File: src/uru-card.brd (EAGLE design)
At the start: 54 x 85.6 mm, 40 parts, among them U1 ESP32-PICO-D4, U2 MPR121QR2, U3 AP2112K-3.3TRG1, U6 ATECC508A-UDFN

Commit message: Added FT260Q USB I2C
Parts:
- added R7, R8: 22, rcl:R0603
- added R9: 5.1k, rcl:R0603
- added U4: FT260Q-T, FT260Q-T:QFN50P500X500X80-29N
- moved C6 2.37 mm to (39.6, 12.1)
- moved R2 2.37 mm to (41.6, 12.1)
- moved U2 2.12 mm to (42.0, 16.0)
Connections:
- removed net VCC: C10.1, U$1.1, U3.1, U3.3
- new net D+: R8.1, U$1.3
- new net D-: R7.1, U$1.2
- new net EXP: U4.29
- new net FSOURCE: U4.25
- new net HID_IRQ: U1.12, U4.15
- new net N$17: R9.2, U4.26
- new net N$5: R7.2, U4.20
- new net N$9: R8.2, U4.21
- new net VBUS: C10.1, R9.1, U$1.1, U3.1, U3.3
- net +3V3: now also U4.1, U4.2, U4.22, U4.23, U4.4, U4.6
- net GND: now also U4.19, U4.24, U4.5
- net RST: now also U4.3
- net SCL: now also U4.12
- net SDA: now also U4.13
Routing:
- net TOUCH_IRQ: track 36.4 -> 5.35 mm, vias 2 -> 1
- net SDA: track 105.3 -> 90.6 mm, vias 3 -> 1
- net SCL: track 104.3 -> 89.7 mm, vias 2 -> 1
- net VCC: track 13.8 -> 0.00 mm
- net VBUS: track 0.00 -> 13.8 mm
- net D+: track 0.00 -> 11.4 mm
- net D-: track 0.00 -> 10.7 mm
- net N$9: track 0.00 -> 5.33 mm
- net N$5: track 0.00 -> 4.69 mm
- net N$17: track 0.00 -> 2.90 mm
- net 8: track 35.2 -> 33.0 mm
- net 9: track 45.1 -> 42.9 mm
- net 5: track 48.3 -> 46.2 mm
- net 4: track 38.3 -> 36.2 mm
- net 3: track 72.4 -> 70.2 mm
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
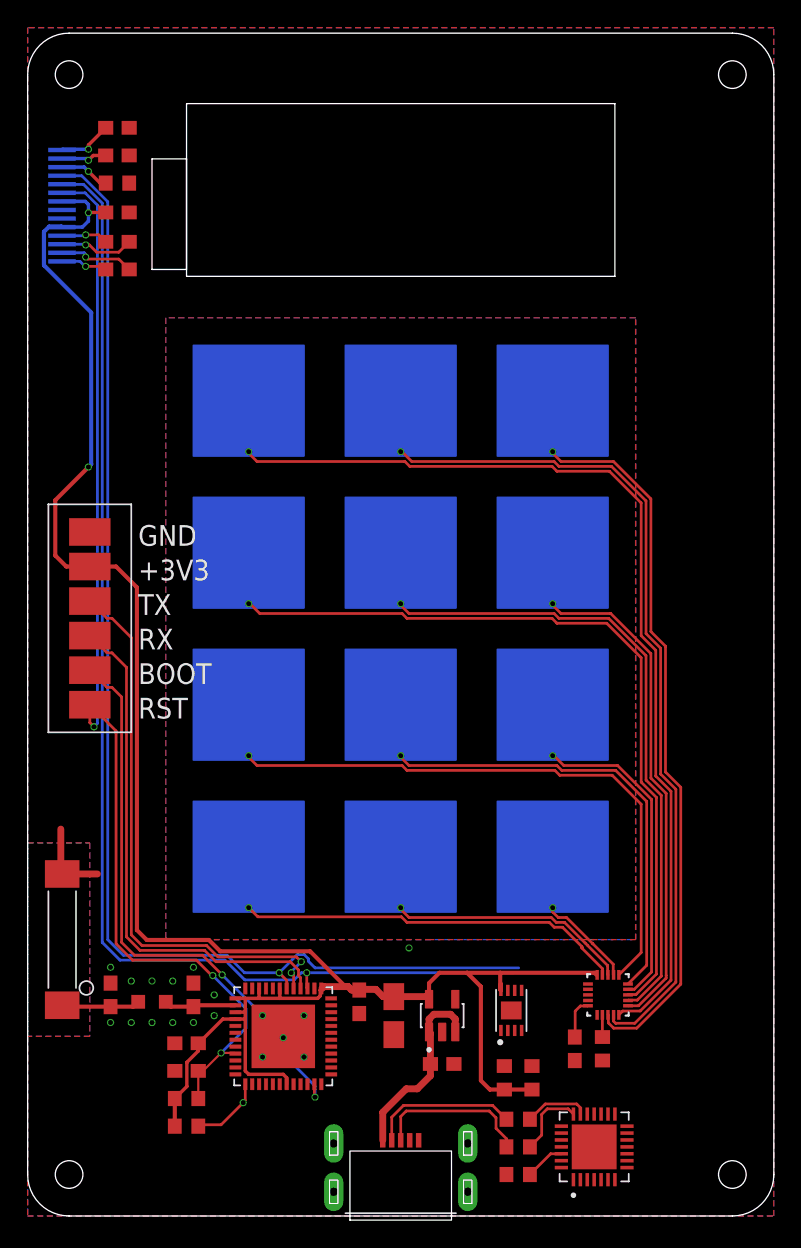
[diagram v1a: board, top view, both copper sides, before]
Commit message: Routed USB HID
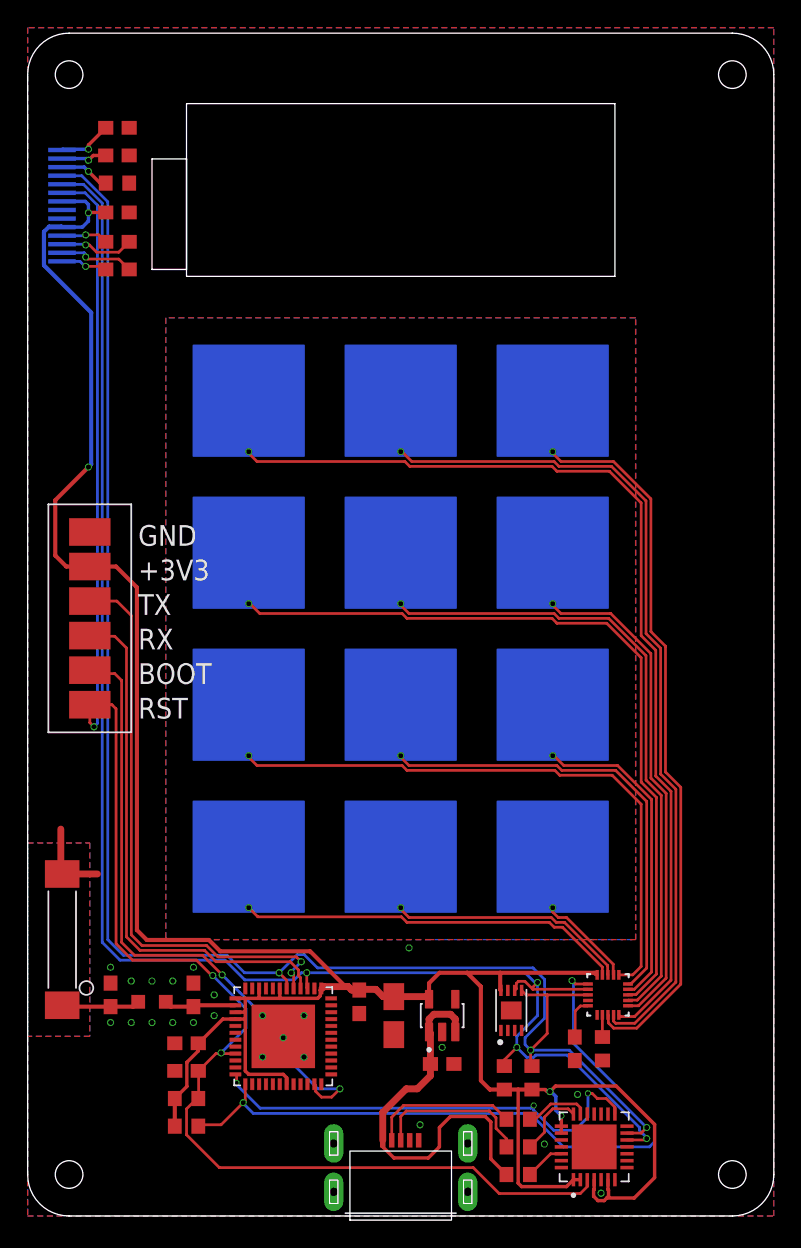
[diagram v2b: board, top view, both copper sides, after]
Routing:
- net TOUCH_IRQ: track 5.35 -> 52.0 mm, vias 1 -> 2
- net +3V3: track 147.1 -> 183.6 mm, vias 2 -> 4
- net RST: track 81.1 -> 116.6 mm
- net HID_IRQ: track 0.00 -> 33.0 mm, vias 0 -> 3
- net SDA: track 90.6 -> 121.6 mm, vias 1 -> 3
- net SCL: track 89.7 -> 119.0 mm, vias 1 -> 4
- net VBUS: track 13.8 -> 29.0 mm
- net IO0: track 41.7 -> 45.3 mm
- net TXD: track 41.0 -> 42.0 mm
- net RXD: track 37.9 -> 38.8 mm
- net 9: track 42.9 -> 43.5 mm
- net GND: track 5.84 -> 5.98 mm, vias 18 -> 23

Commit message: Changed routing for the display component
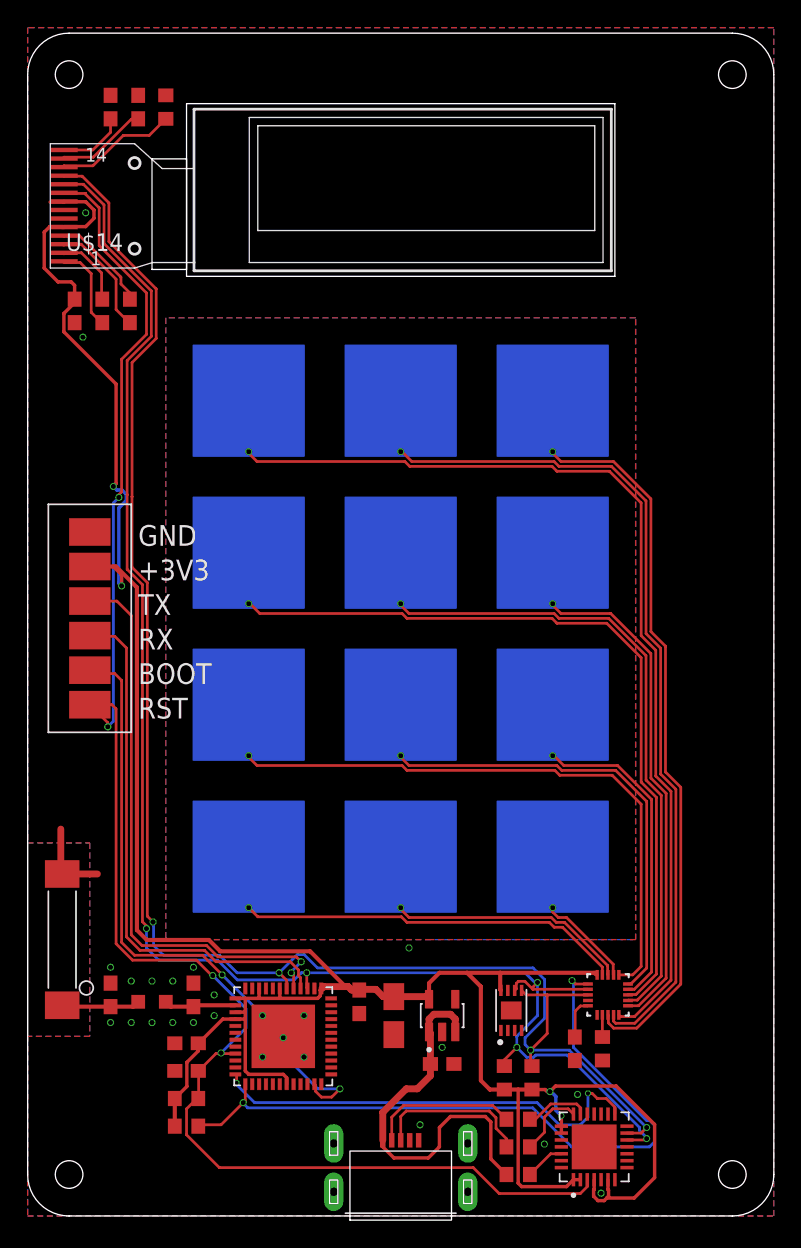
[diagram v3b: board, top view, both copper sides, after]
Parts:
- U$14: value WEO012832F -> WEO012832FREVERSED; device OLED:WEO012832F-CONN -> OLED:WEO012832F-REVERSE
- moved U$14 40.5 mm to (1.50, 80.0), flipped to the top
- moved C13 7.77 mm to (3.40, 65.5), turned to 270 degrees
- moved R4 6.52 mm to (10.0, 80.2), turned to 270 degrees
- moved C9 5.08 mm to (7.40, 65.5), turned to 270 degrees
- moved C12 3.81 mm to (8.00, 80.2), turned to 90 degrees
- moved C7 3.20 mm to (5.40, 65.5), turned to 270 degrees
- moved C11 1.58 mm to (6.00, 80.2), turned to 90 degrees
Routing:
- net N$6: track 3.64 -> 8.90 mm, vias 1 -> 0
- net +3V3: track 183.6 -> 188.3 mm
- net N$1: track 3.40 -> 7.30 mm, vias 1 -> 0
- net N$7: track 3.36 -> 6.64 mm, vias 1 -> 0
- net N$2: track 5.42 -> 8.59 mm, vias 1 -> 0
- net RST: track 116.6 -> 119.7 mm, vias 3 -> 4
- net N$4: track 3.43 -> 6.40 mm, vias 1 -> 0
- net N$8: track 4.01 -> 4.91 mm, vias 1 -> 0
- net HID_IRQ: track 33.0 -> 32.3 mm, vias 3 -> 2
- net SDA: track 121.6 -> 121.2 mm, vias 3 -> 4
- net SCL: track 119.0 -> 118.8 mm, vias 4 -> 5
- net N$3: track 5.48 -> 5.36 mm, vias 1 -> 0
- net GND: vias 23 -> 25

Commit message: Design refactoring
Replaced the antenna with PCB one
Moved connector
Replaced tantalum capacitor with ceramic ones
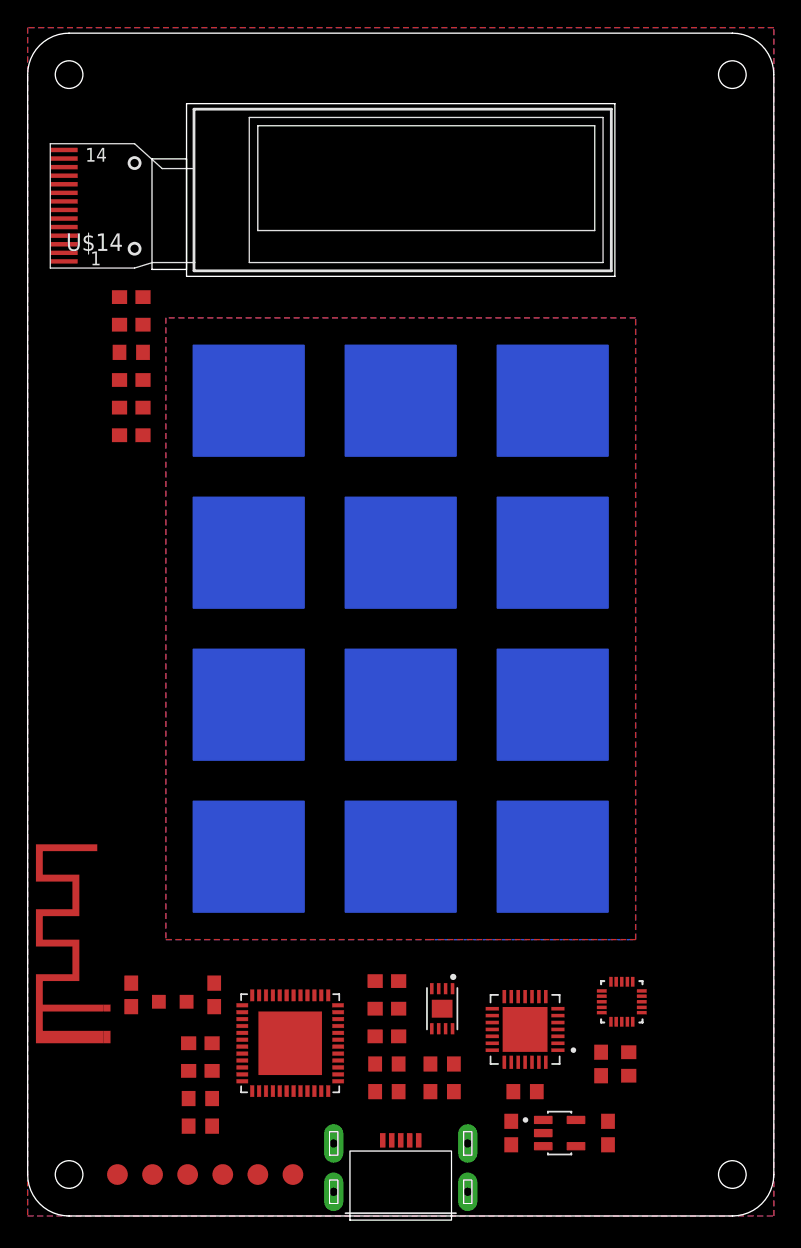
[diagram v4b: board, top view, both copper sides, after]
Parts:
- removed ANT1: AN9520, AN9520:SMD_ANT9520
- added C14, C15: 10u, rcl:C0603
- added U$16: CONNPADS, CONN:PADS
- C2: value 100u -> 10u; device rcl:A/3216-18R -> rcl:C0603
- U$15: value PROG -> ANT-2_4_PCB; device pads:PADS-6 -> ANT:ANT-2_4
- moved U$15 30.5 mm to (5.50, 12.5), turned to 90 degrees
- moved C8 20.4 mm to (42.0, 6.00)
- moved R4 17.9 mm to (7.50, 62.5), turned to 180 degrees
- moved C12 15.8 mm to (7.50, 64.5), turned to 0 degrees
- moved C11 13.8 mm to (7.50, 66.5), turned to 0 degrees
- moved U3 12.0 mm to (38.5, 6.00), turned to 0 degrees
- moved R5 10.5 mm to (26.0, 11.0), turned to 180 degrees
- moved U4 9.86 mm to (36.0, 13.5), turned to 180 degrees
- moved C7 9.24 mm to (7.50, 56.5), turned to 0 degrees
- moved R6 8.56 mm to (26.0, 9.00), turned to 180 degrees
- moved C10 7.07 mm to (35.0, 6.00), turned to 270 degrees
- moved C9 7.00 mm to (7.50, 58.5), turned to 0 degrees
- moved R7 6.80 mm to (30.0, 11.0)
- moved R8 6.80 mm to (30.0, 9.00)
- moved C13 6.47 mm to (7.50, 60.5), turned to 0 degrees
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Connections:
- net +3V3: now also C14.1, C15.1, C2.1, U$16.P$5; no longer C2.+, U$15.P5
- net ANT_FEED: now also U$15.FEED; no longer ANT1.P$FEED
- net GND: now also C14.2, C15.2, C2.2, U$15.GND, U$16.P$6; no longer ANT1.P$GND, C2.-, U$15.P6
- net IO0: now also U$16.P$2; no longer U$15.P2
- net RST: now also U$16.P$1; no longer U$15.P1
- net RXD: now also U$16.P$3; no longer U$15.P3
- net TXD: now also U$16.P$4; no longer U$15.P4
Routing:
- net +3V3: track 188.3 -> 0.00 mm, vias 4 -> 0
- net SDA: track 121.2 -> 0.00 mm, vias 4 -> 0
- net RST: track 119.7 -> 0.00 mm, vias 4 -> 0
- net SCL: track 118.8 -> 0.00 mm, vias 5 -> 0
- net 3: track 70.3 -> 0.00 mm, vias 1 -> 0
- net 2: track 61.2 -> 0.00 mm, vias 1 -> 0
- net 6: track 56.2 -> 0.00 mm, vias 1 -> 0
- net TOUCH_IRQ: track 52.2 -> 0.00 mm, vias 2 -> 0
- net 1: track 51.9 -> 0.00 mm, vias 1 -> 0
- net 5: track 46.2 -> 0.00 mm, vias 1 -> 0
- net IO0: track 45.3 -> 0.00 mm, vias 2 -> 0
- net 9: track 43.5 -> 0.00 mm, vias 1 -> 0
- net TXD: track 42.0 -> 0.00 mm, vias 2 -> 0
- net RXD: track 38.8 -> 0.00 mm
- net 4: track 36.2 -> 0.00 mm, vias 1 -> 0
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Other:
- board text removed: "+3V3"
- board text removed: "BOOT"
- board text removed: "GND"
- board text removed: "RST"
- board text removed: "RX"
- board text removed: "TX"

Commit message: v1.1
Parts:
- moved L2 0.50 mm to (10.5, 15.0)
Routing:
- net +3V3: track 0.00 -> 183.2 mm, vias 0 -> 9
- net RST: track 0.00 -> 117.9 mm, vias 0 -> 6
- net SCL: track 0.00 -> 109.8 mm, vias 0 -> 4
- net SDA: track 0.00 -> 106.7 mm, vias 0 -> 7
- net 3: track 0.00 -> 72.0 mm, vias 0 -> 1
- net 2: track 0.00 -> 63.1 mm, vias 0 -> 1
- net TOUCH_IRQ: track 0.00 -> 60.3 mm, vias 0 -> 2
- net 6: track 0.00 -> 57.6 mm, vias 0 -> 1
- net 1: track 0.00 -> 53.9 mm, vias 0 -> 1
- net 5: track 0.00 -> 47.7 mm, vias 0 -> 1
- net 9: track 0.00 -> 44.1 mm, vias 0 -> 1
- net 4: track 0.00 -> 37.9 mm, vias 0 -> 1
- net HID_IRQ: track 0.00 -> 36.7 mm, vias 0 -> 2
- net 8: track 0.00 -> 34.1 mm, vias 0 -> 1
- net OK: track 0.00 -> 29.1 mm, vias 0 -> 1
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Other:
- board text added: "Security Development Platform"
- board text added: "https://en.ovcharov.me/"
- board text removed: "ESP32 Security Development Platform v1"

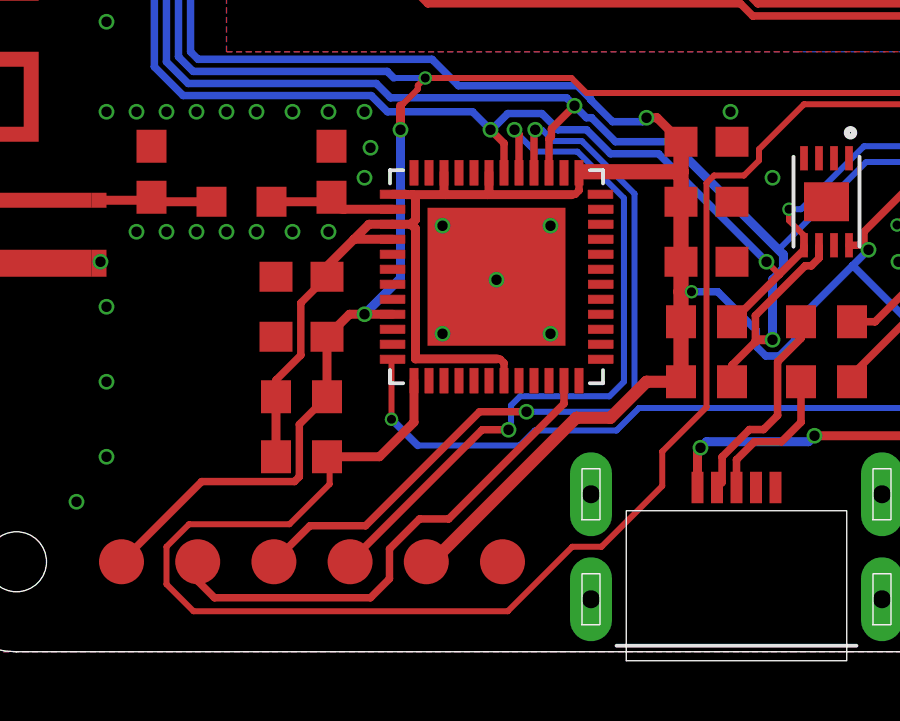
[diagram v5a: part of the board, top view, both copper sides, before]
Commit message: fixed the trace crossing cut out
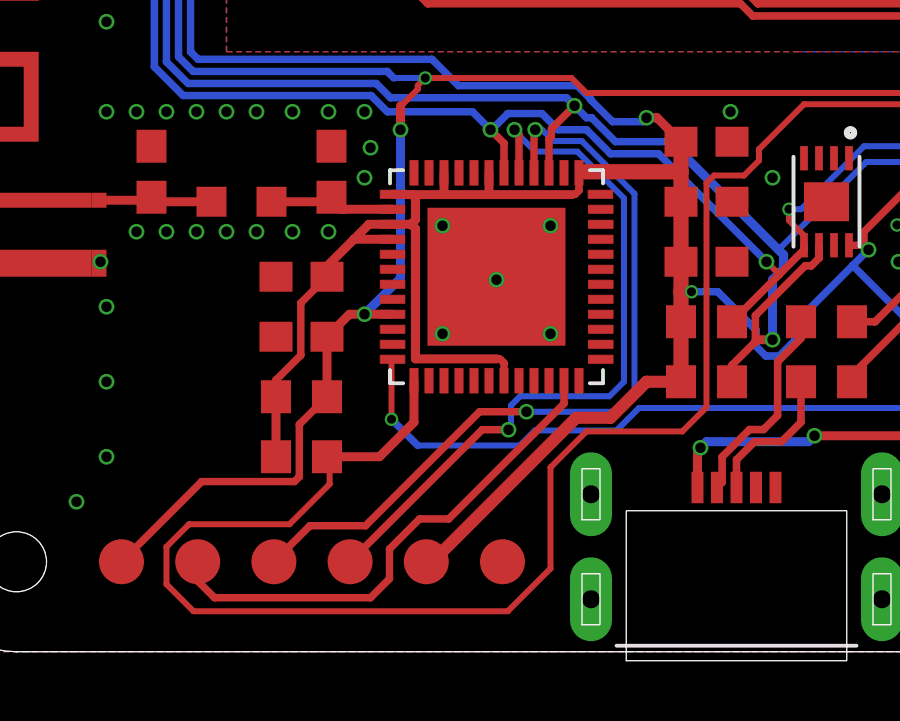
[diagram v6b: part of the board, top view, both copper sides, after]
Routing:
- net TOUCH_IRQ: track 60.3 -> 61.6 mm
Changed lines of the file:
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@@
 <wire x1="26.25" y1="15.875" x2="27.25" y2="15.875" width="0.2" layer="1"/>
 <wire x1="26" y1="15.625" x2="26.25" y2="15.875" width="0.2" layer="1"/>
-<wire x1="26" y1="8.15" x2="26" y2="15.625" width="0.2" layer="1"/>
-<wire x1="24.525" y1="6.675" x2="26" y2="8.15" width="0.2" layer="1"/>
-<wire x1="24.525" y1="5.525" x2="24.525" y2="6.675" width="0.2" layer="1"/>
-<wire x1="22.5" y1="3.5" x2="24.525" y2="5.525" width="0.2" layer="1"/>
-<wire x1="21.525" y1="3.5" x2="22.5" y2="3.5" width="0.2" layer="1"/>
-<wire x1="19.375" y1="1.35" x2="21.525" y2="3.5" width="0.2" layer="1"/>
-<wire x1="8.9" y1="1.35" x2="19.375" y2="1.35" width="0.2" layer="1"/>
+<wire x1="26" y1="15.625" x2="26" y2="8.15" width="0.2" layer="1"/>
+<wire x1="19.375" y1="1.35" x2="8.9" y2="1.35" width="0.2" layer="1"/>
 <wire x1="8" y1="2.25" x2="8.9" y2="1.35" width="0.2" layer="1"/>
 <wire x1="8" y1="3.5" x2="8" y2="2.25" width="0.2" layer="1"/>
@@
 <wire x1="41.5522" y1="16.2874" x2="39.4626" y2="16.2874" width="0.2" layer="1"/>
 <wire x1="39.4626" y1="16.2874" x2="38.875" y2="16.875" width="0.2" layer="1"/>
+<wire x1="26" y1="8.15" x2="25.1944" y2="7.3444" width="0.2" layer="1"/>
+<wire x1="25.1944" y1="7.3444" x2="22" y2="7.3444" width="0.2" layer="1"/>
+<wire x1="22" y1="7.3444" x2="20.8" y2="6.1444" width="0.2" layer="1"/>
+<wire x1="20.8" y1="2.775" x2="19.375" y2="1.35" width="0.2" layer="1"/>
+<wire x1="20.8" y1="6.1444" x2="20.8" y2="2.775" width="0.2" layer="1"/>
 </signal>
 <signal name="N$18">
